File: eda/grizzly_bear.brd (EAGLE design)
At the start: 76.2 x 41.3 mm, 65 parts, among them Q1 PSMN4R0, Q2 PSMN4R0, Q3 PSMN4R0, Q4 PSMN4R0, Q5 IPD90P03P4L, U1 A4940, U2 ATMEGA32U4-AU, U3 ACS714, U4 UA78L00, U5 ISL83491SOIC, Y1 16MHz

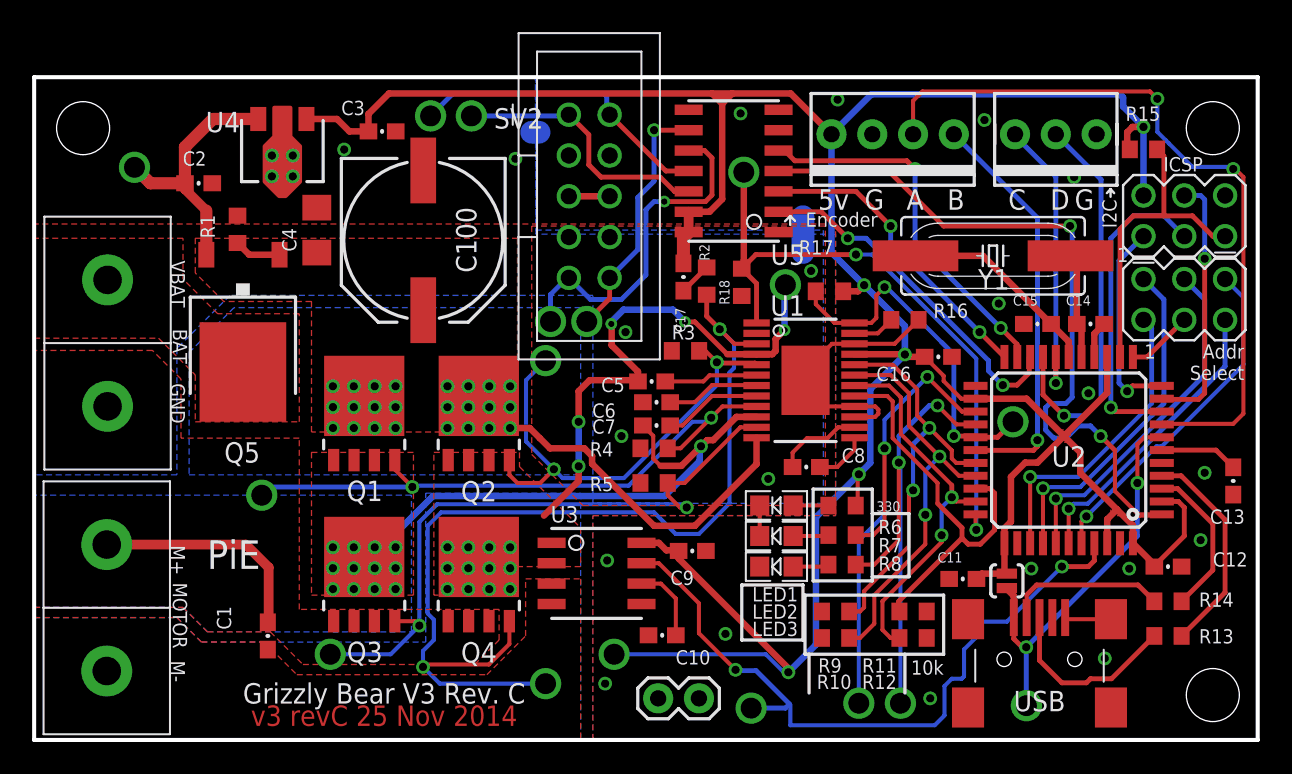
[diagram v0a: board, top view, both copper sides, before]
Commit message: Replace USB Mini with USB Micro AB on board, clean up traces and silkscreen
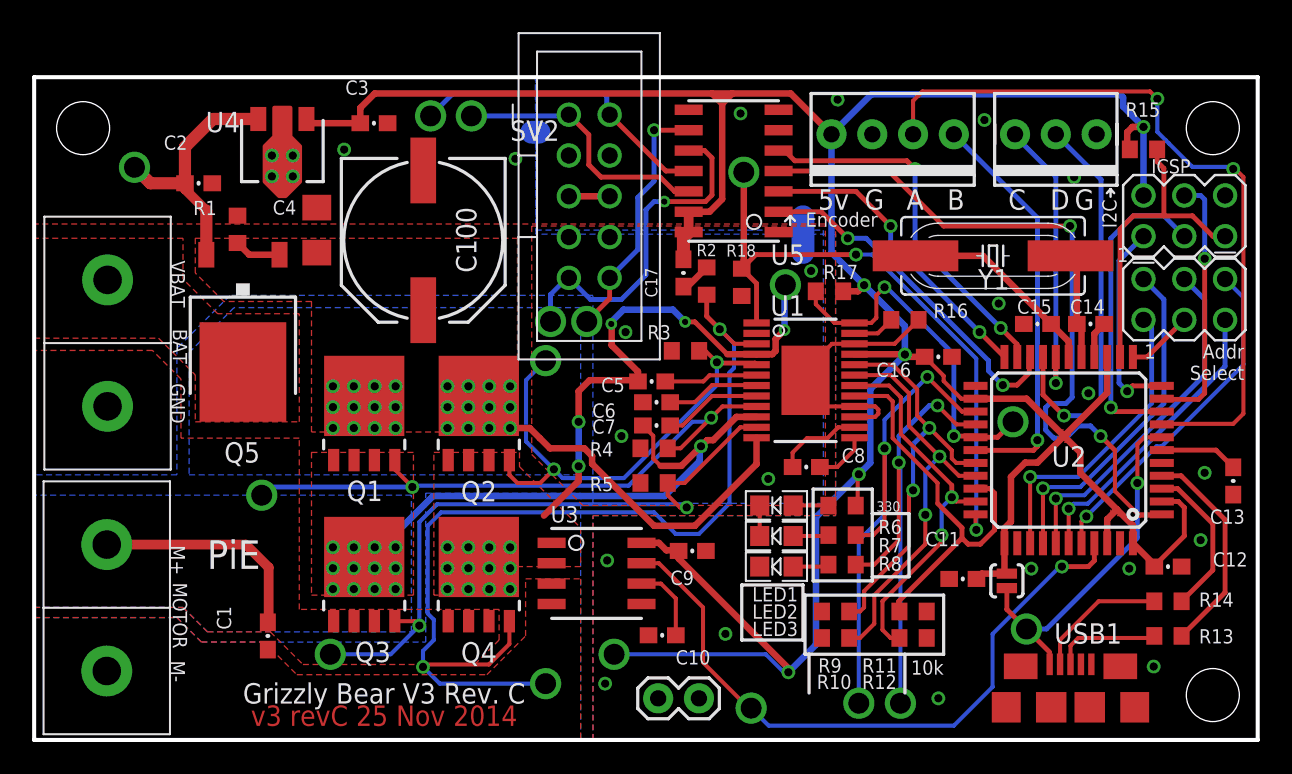
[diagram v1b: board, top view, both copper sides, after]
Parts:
- removed U$2: USB-M26FTR, pie:USB-M26FTR
- added USB1: USB-OTGMICRO-AB, pie:USB-MICRO-AB
- moved C3 0.72 mm to (21.2, 38.4)
- moved C17 0.25 mm to (40.4, 29.1)
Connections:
- net D+-_CON: now also USB1.P$3; no longer U$2.D+
- net D-_CON: now also USB1.P$2; no longer U$2.D-
- net GND: now also USB1.P$10, USB1.P$11, USB1.P$5, USB1.P$6, USB1.P$7, USB1.P$8, USB1.P$9; no longer U$2.G, U$2.S1, U$2.S2, U$2.S3, U$2.S4
- net VUSB: now also USB1.P$1; no longer U$2.5V
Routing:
- net D+-_CON: track 11.6 -> 6.63 mm
- net GND: track 32.5 -> 29.5 mm
- net ISENSE: track 44.5 -> 41.7 mm, vias 3 -> 2
- net VUSB: track 25.2 -> 22.7 mm, vias 3 -> 2
- net D-_CON: track 10.0 -> 8.39 mm
- net 5V: track 197.3 -> 196.5 mm

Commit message: Grizzly merge fix
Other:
- board text added: "Grizzly Bear V4 Rev. A"
- board text added: "v4 revA 26 Nov 2015"
- board text removed: "Grizzly Bear V3 Rev. C"
- board text removed: "v3 revC 25 Nov 2014"
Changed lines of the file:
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@@
 <layer number="20" name="Dimension" color="15" fill="1" visible="yes" active="yes"/>
 <layer number="21" name="tPlace" color="16" fill="1" visible="yes" active="yes"/>
-<layer number="22" name="bPlace" color="17" fill="1" visible="no" active="yes"/>
+<layer number="22" name="bPlace" color="17" fill="1" visible="yes" active="yes"/>
 <layer number="23" name="tOrigins" color="15" fill="1" visible="yes" active="yes"/>
 <layer number="24" name="bOrigins" color="15" fill="1" visible="yes" active="yes"/>
@@
 <text x="9.525" y="24.511" size="0.889" layer="21" font="vector" ratio="15" rot="SR270" align="top-center">BAT</text>
 <text x="9.525" y="7.747" size="0.889" layer="21" font="vector" ratio="15" rot="SR270" align="top-center">MOTOR</text>
-<text x="21.7932" y="0.874" size="1.27" layer="1" font="vector" ratio="15" align="bottom-center">v3 revC 25 Nov 2014</text>
-<text x="21.7932" y="2.2652" size="1.27" layer="21" font="vector" ratio="15" align="bottom-center">Grizzly Bear V3 Rev. C</text>
+<text x="21.7932" y="0.874" size="1.27" layer="1" font="vector" ratio="15" align="bottom-center">v4 revA 26 Nov 2015</text>
+<text x="21.7932" y="2.2652" size="1.27" layer="21" font="vector" ratio="15" align="bottom-center">Grizzly Bear V4 Rev. A</text>
 <text x="10.766" y="10.65" size="1.778" layer="21" font="vector" ratio="15">PiE</text>
 <text x="75.3618" y="24.638" size="0.889" layer="21" font="vector" ratio="20" align="top-right">Addr
@@
 <element name="JP1" library="SparkFun-Connectors" package="1X02" value="M02PTH" x="38.862" y="2.5908" smashed="yes"/>
 <element name="USB1" library="pie" package="USB-MICRO-AB" value="USB-OTGMICRO-AB" x="64.5414" y="3.7084" smashed="yes">
-<attribute name="DIGIKEY-PN" value="H11635CT-ND" x="64.5414" y="3.7084" size="1.778" layer="27" display="off"/>
 <attribute name="PIE-INT-REF-NUM" value="USB" x="64.5414" y="3.7084" size="1.778" layer="27" display="off"/>
 <attribute name="NAME" x="63.5254" y="5.9944" size="1.27" layer="25" font="vector" ratio="10"/>
+<attribute name="PIE-DIGIKEY-PN-PRI" value="H11635CT-ND" x="64.5414" y="3.7084" size="1.778" layer="27" display="off"/>
 </element>
 </elements>
@@
 <via x="61.7982" y="6.9088" extent="1-16" drill="1.3"/>
 <contactref element="USB1" pad="P$1"/>
-<wire x1="63.2414" y1="4.7084" x2="63.2414" y2="5.4656" width="0.254" layer="1"/>
+<wire x1="63.2414" y1="4.7084" x2="63.2414" y2="5.4656" width="0.3048" layer="1"/>
 <wire x1="63.2414" y1="5.4656" x2="61.7982" y2="6.9088" width="0.3048" layer="1"/>
 <wire x1="61.7982" y1="6.9088" x2="60.579" y2="8.128" width="0.3048" layer="1"/>
